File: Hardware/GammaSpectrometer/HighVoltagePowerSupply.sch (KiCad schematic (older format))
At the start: 59 parts, among them J1 power supply, J4 Conn_01x07_Female, J5 RF_Shield_Two_Pieces, Q1 AOD2810, U1 MCP1416

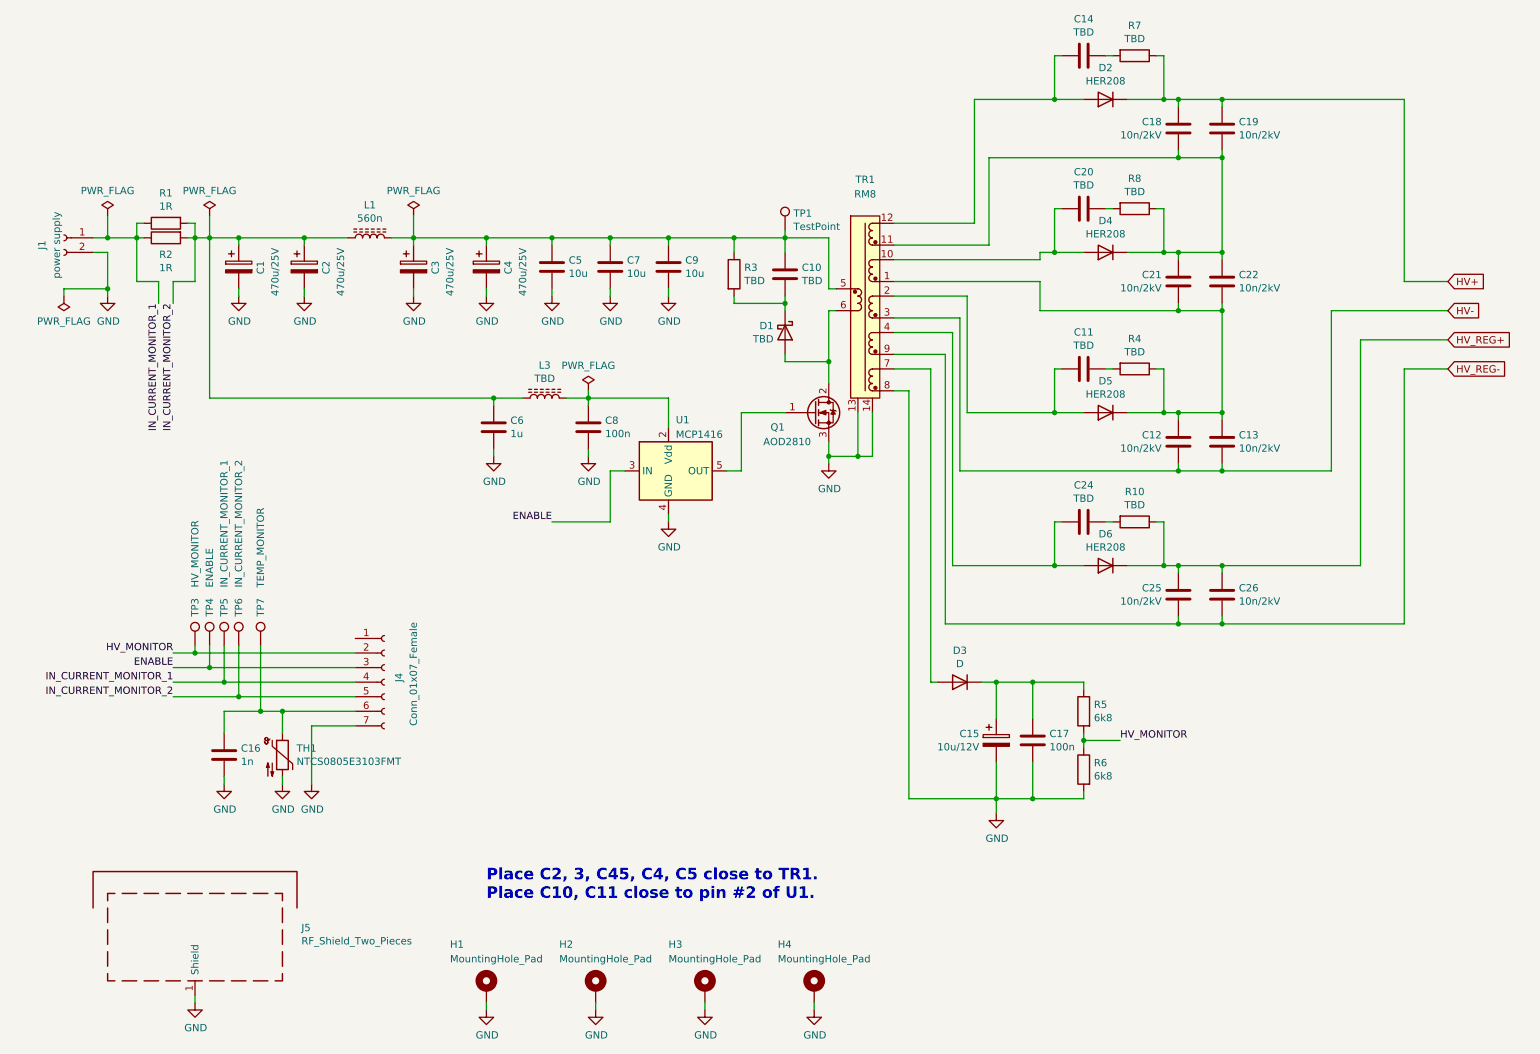
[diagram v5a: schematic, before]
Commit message: draft of component placement on PCB
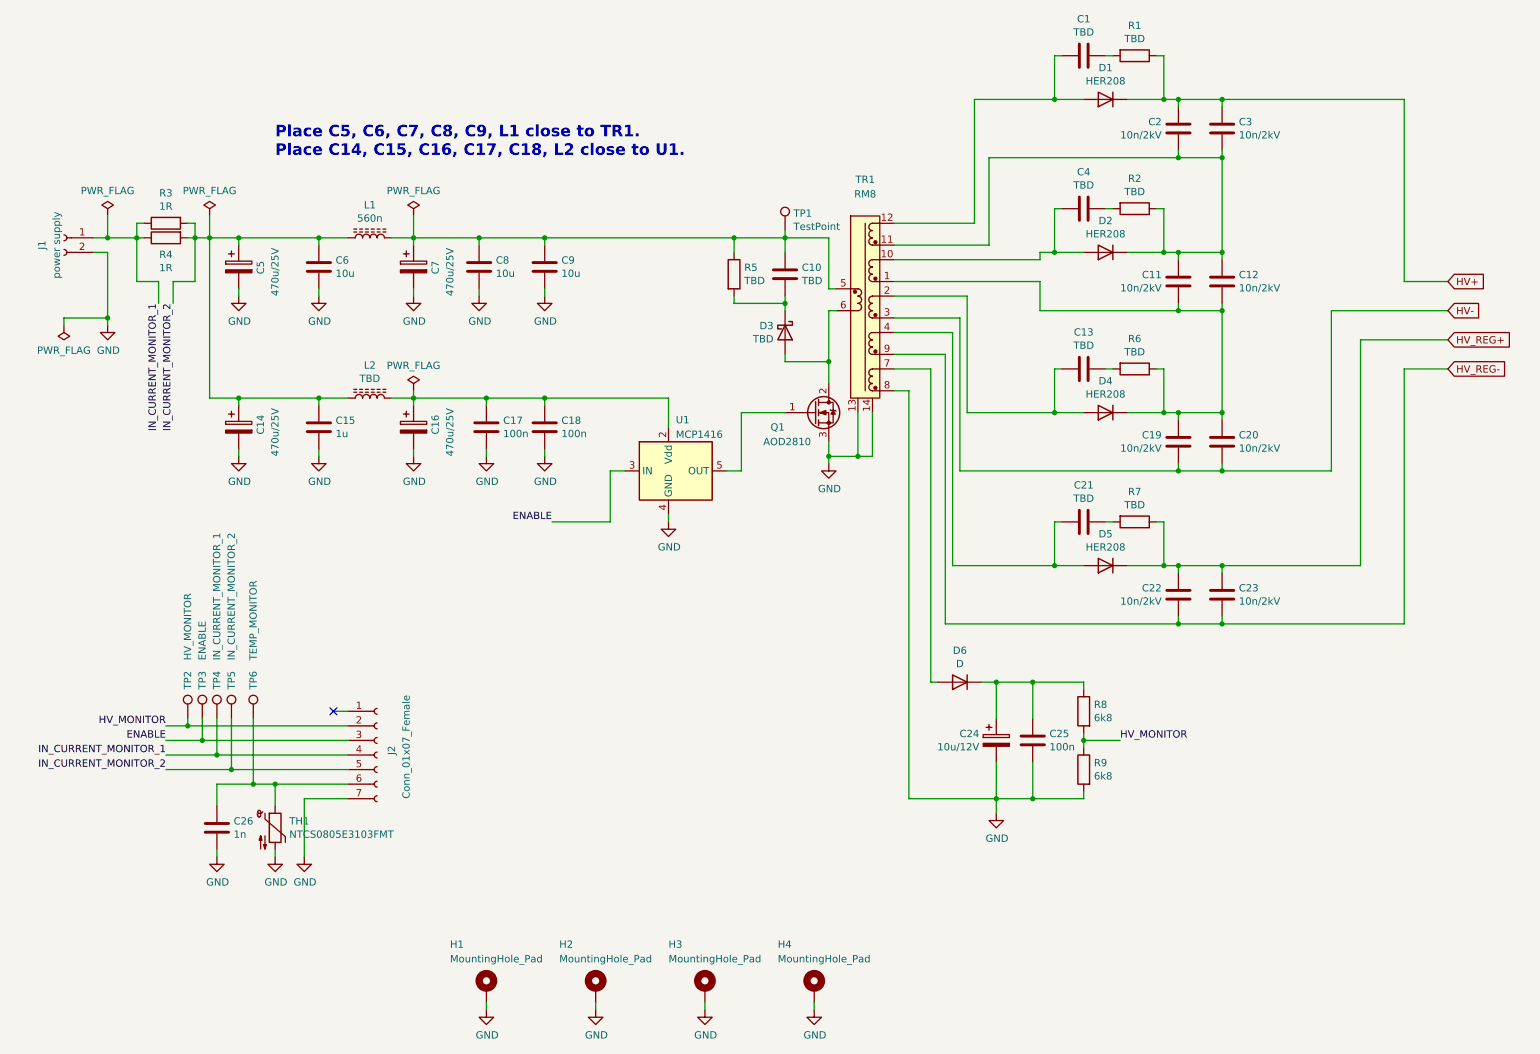
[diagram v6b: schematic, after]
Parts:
- removed C2, C4: 470u/25V, Capacitor_SMD:CP_Elec_10x10, symbol Device:CP
- removed J5: RF_Shield_Two_Pieces, GammaSpectrometer:3710.16, symbol Device:RF_Shield_Two_Pieces
- added C14, C16: 470u/25V, Capacitor_SMD:CP_Elec_10x10, symbol Device:CP
- added C18: 100n, Capacitor_SMD:C_1206_3216Metric, symbol Device:C
- D1: renamed from D2; footprint (none) -> Diode_SMD:D_MiniMELF
- D2: renamed from D4; footprint (none) -> Diode_SMD:D_MiniMELF
- D3: renamed from D1; footprint Diode_SMD:D_SMB -> Diode_SMD:D_MiniMELF
- D4: renamed from D5; footprint (none) -> Diode_SMD:D_MiniMELF
- D5: renamed from D6; footprint (none) -> Diode_SMD:D_MiniMELF
- D6: renamed from D3; footprint (none) -> Diode_SMD:D_MiniMELF
- J1: footprint GammaSpectrometer:DG300-5.0-02P-12-00A(H) -> Connector_PinSocket_2.54mm:PinSocket_1x02_P2.54mm_Vertical_SMD_Pin1Left
- L1: footprint Inductor_SMD:L_10.4x10.4_H4.8 -> Inductor_SMD:L_12x12mm_H6mm
- L2: renamed from L3; footprint (none) -> Inductor_SMD:L_12x12mm_H6mm
- renumbered C14 to C1, C21 to C11, C22 to C12, C11 to C13, C6 to C15, C8 to C17, C12 to C19, C18 to C2, C13 to C20, C24 to C21, C25 to C22, C26 to C23, C15 to C24, C17 to C25, C16 to C26, C19 to C3, C20 to C4, C1 to C5, C5 to C6, C3 to C7, C7 to C8, J4 to J2, R7 to R1, R8 to R2, R1 to R3, R2 to R4, R3 to R5, R4 to R6, R10 to R7, R5 to R8, R6 to R9, TP3 to TP2, TP4 to TP3, TP5 to TP4, TP6 to TP5, TP7 to TP6
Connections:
- net GND: now also C14.2, C16.2, C18.1
- net IN_CURRENT_MONITOR_2: now also C6.2, C14.1
- net at C10.2, C7.1, C8.2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: no longer C6.2
- net at C17.2, L2.2, U1.2 (Vdd): now also C16.1, C18.2
- no-connect marks 0 -> 1
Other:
- note added: "Place C5, C6, C7, C8, C9, L1 close to TR1.\nPlace C14, C15, C16, C17, C18, L2 close to U1."
- note removed: "Place C2, 3, C45, C4, C5 close to TR1.\nPlace C10, C11 close to pin #2 of U1.\n"
- moved on the sheet: C15, C17, C26, C6, C8, C9, J2, L2, TH1, TP2, TP3, TP4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
